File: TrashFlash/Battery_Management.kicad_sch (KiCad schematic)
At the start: 18 parts, among them IC10 BQ24230RGTR, IC3 BQ27426YZFR, IC9 BQ29732DSER, J1 USB4800-03-A, Q5 PMDPB30XNAX

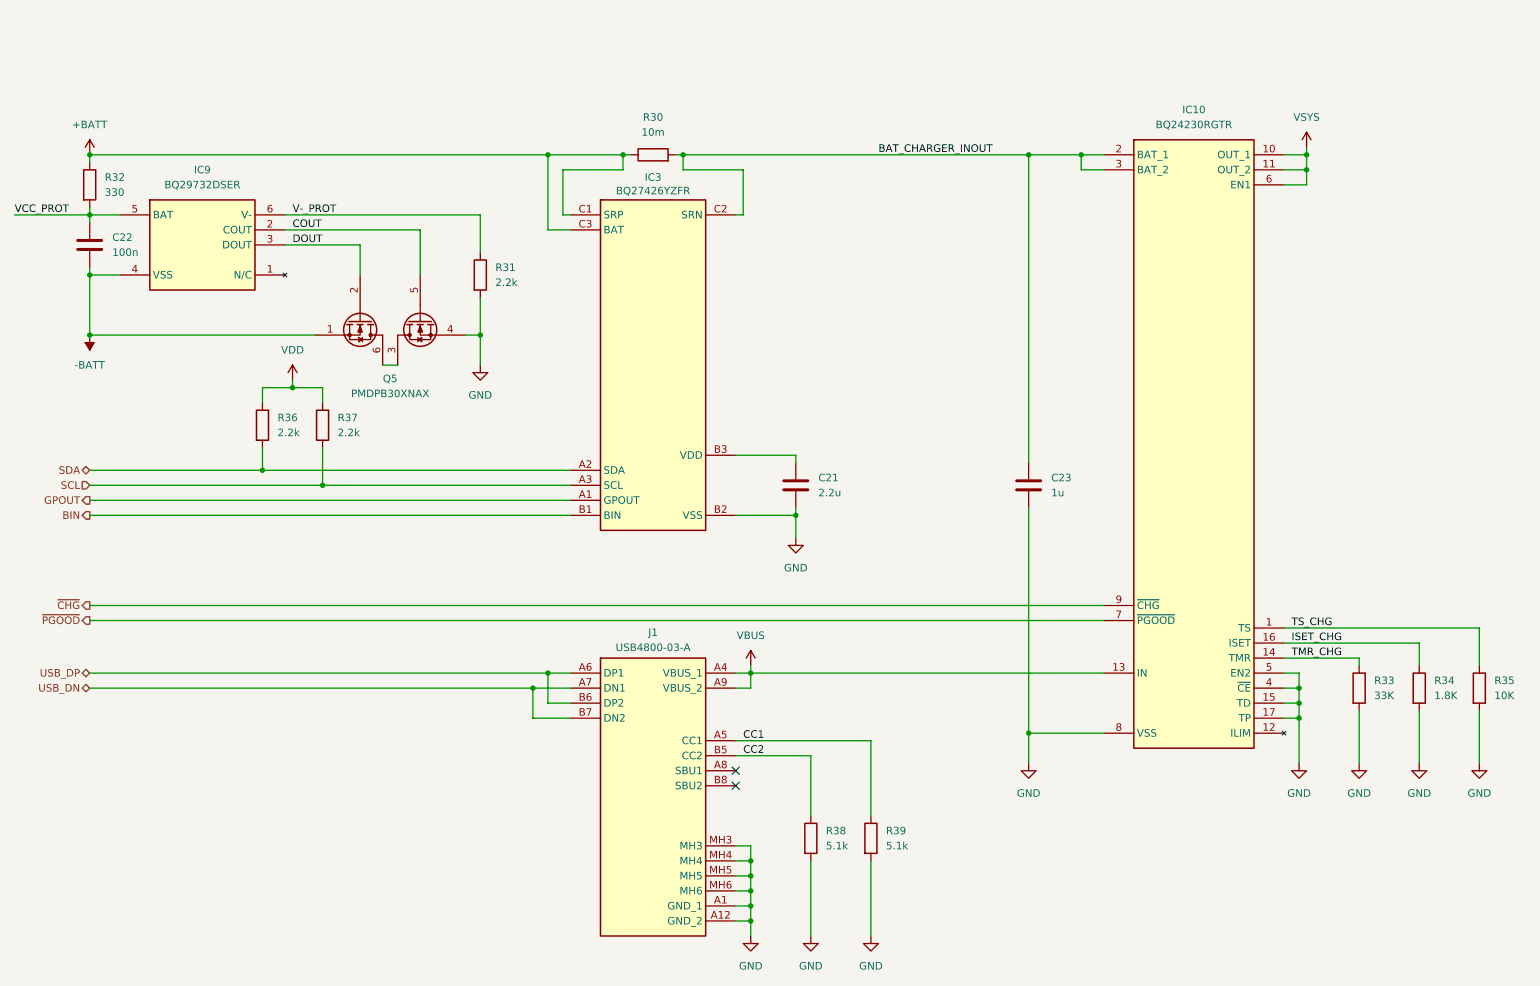
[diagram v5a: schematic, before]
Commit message: Added Wireless and inter PCB connector
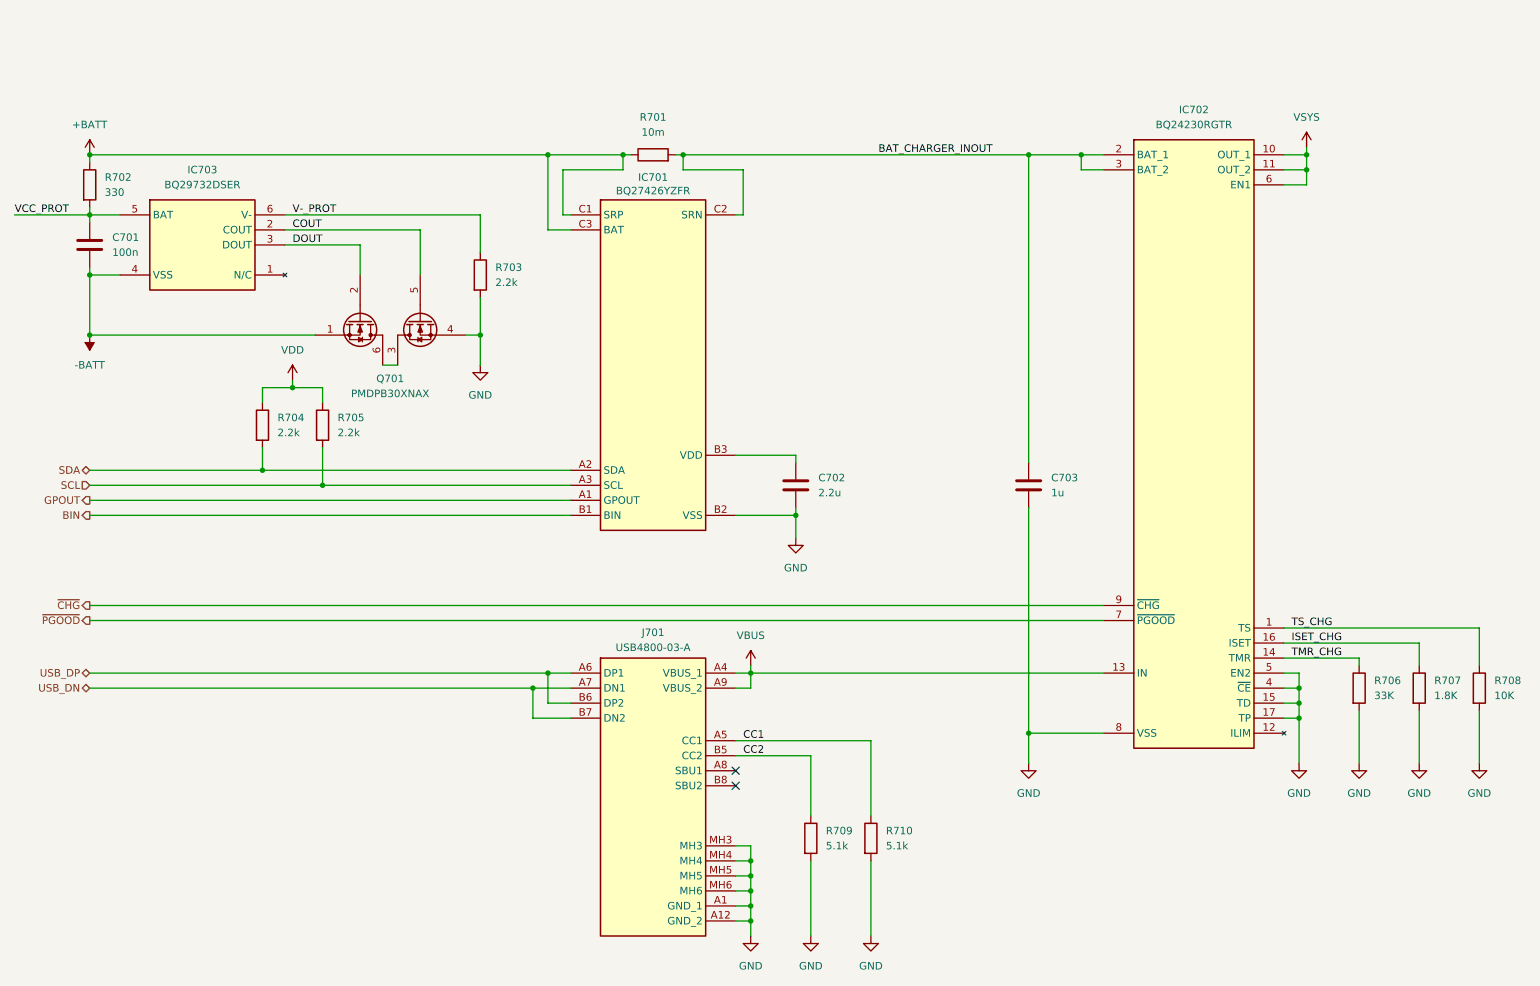
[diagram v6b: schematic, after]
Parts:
- IC701: renamed from IC3; footprint TrashFlash:BGA9C50P3X3_158X162X62 -> BGA9C50P3X3_158X162X62
- IC702: renamed from IC10; footprint TrashFlash:QFN50P300X300X100-17N-D -> QFN50P300X300X100-17N-D
- IC703: renamed from IC9; footprint TrashFlash:SON50P150X150X80-6N -> SON50P150X150X80-6N
- J701: renamed from J1; footprint TrashFlash:USB480003A -> USB480003A
- Q701: renamed from Q5; footprint TrashFlash:PMDPB30XNAX -> PMDPB30XNAX
- renumbered C22 to C701, C21 to C702, C23 to C703, R30 to R701, R32 to R702, R31 to R703, R36 to R704, R37 to R705, R33 to R706, R34 to R707, R35 to R708, R38 to R709, R39 to R710
